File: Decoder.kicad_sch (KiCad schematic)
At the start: 10 parts, among them P1 IO_ADDR, P17 RTC_IO_ADDR, U2 74LS14, U21 74LS682N, U33 74LS10, U39 74LS04, U57 74LS682N, U58 74LS138, U68 74LS138, U7 74LS32

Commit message: rev 1.0
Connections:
- net /CS_FP: now reaches U58.13 (O2)
- net EXTIORQ renamed /INTIORQ
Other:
- note added: "80-83 8242 KBD 84-87 PPI2 88-8B open 8C-8F FDC 90-93 UTIL 94-97 ACRRCS 98-9B VDPCS 9C-9F SNDCS"
- note removed: "80-83 ppi1 84-87 PPI2 88-8B open 8C-8F FDC 90-93 UTIL 94-97 ACRRCS 98-9B VDPCS 9C-9F SNDCS"
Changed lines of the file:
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@@
 	(title_block
 		(title "N8PC")
-		(date "2025-11-02")
-		(rev "000.8")
+		(date "2025-11-26")
+		(rev "000.9")
 		(comment 1 "https://github.com/danwerner21/N8PC")
 		(comment 2 "Based on work by Andrew Lynch and John Coffman")
@@
 		)
 	)
-	(text "80-83 ppi1\n84-87 PPI2\n88-8B open\n8C-8F FDC\n90-93 UTIL\n94-97 ACRRCS\n98-9B VDPCS\n9C-9F SNDCS\n"
+	(text "80-83 8242 KBD\n84-87 PPI2\n88-8B open\n8C-8F FDC\n90-93 UTIL\n94-97 ACRRCS\n98-9B VDPCS\n9C-9F SNDCS\n"
 		(exclude_from_sim no)
 		(at 201.676 70.358 0)
@@
 	)
 	(no_connect
-		(at 166.37 50.8)
+		(at 240.03 184.15)
 	)
 	(no_connect
@@
 		(pts
 			(xy 270.51 104.14) (xy 259.08 104.14)
+		)
+		(stroke
+			(width 0)
+			(type default)
+		)
+	)
+	(wire
+		(pts
+			(xy 166.37 50.8) (xy 180.34 50.8)
 		)
 		(stroke
@@
 		)
 	)
+	(global_label "{slash}CS_FP"
+		(shape output)
+		(at 180.34 50.8 0)
+		(fields_autoplaced yes)
+		(effects
+			(font
+				(size 1.27 1.27)
+			)
+			(justify left)
+		)
+		(property "Intersheetrefs" "${INTERSHEET_REFS}"
+			(at 189.8072 50.8 0)
+			(effects
+				(font
+					(size 1.27 1.27)
+				)
+				(justify left)
+				(hide yes)
+			)
+		)
+	)
 	(global_label "{slash}M1"
 		(shape input)
@@
 		)
 	)
-	(global_label "EXTIORQ"
+	(global_label "{slash}INTIORQ"
 		(shape output)
 		(at 134.62 67.31 0)
@@
 		)
 		(property "Intersheetrefs" "${INTERSHEET_REFS}"
-			(at 144.8129 67.31 0)
+			(at 145.7202 67.31 0)
 			(effects
 				(font

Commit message: V1
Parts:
- removed P17: RTC_IO_ADDR, Custom:STD_DDW_PINHEAD_V_2x04, symbol Connector_Generic:Conn_02x04_Odd_Even
- added P16: IO_ADDR2, Custom:STD_DDW_PinHeader_2x03, symbol Connector_Generic:Conn_02x03_Odd_Even
- added unit 5 of U39
- added U5: 74LS02, Custom:STD_DDW_DIP14, symbol 74xx:74LS02
- added U9: 74LS138, Custom:STD_DDW_DIP16, symbol 74xx:74LS138
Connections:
- net A4: now also U9.3 (A2); no longer U21.8 (P3)
- net GND: now also U21.12 (Q4), U21.13 (P5), P16.1 (Pin_1), P16.3 (Pin_3), P16.5 (Pin_5), U9.1 (A0), U9.2 (A1), U9.5 (E2), U9.8 (GND)
- net VCC: now also U21.9 (Q3), U9.16 (VCC), U9.6 (E3); no longer U21.12 (Q4)
- net /CS_RTC: now also U9.11 (O4); no longer U21.19 (~{P=Q})
- net /INTIORQ: now also U39.10; no longer U57.19 (~{P=Q}), U58.4 (E1)
- net /IORQ: now also U21.11 (P4); no longer U21.13 (P5)
- net /M1: now also U21.8 (P3); no longer U21.11 (P4)
- net /SNDCS: now also U9.15 (O0); no longer U58.7 (O7)
- net at U21.3 (Q0): now also P16.2 (Pin_2)
- net at U21.5 (Q1): now also P16.4 (Pin_4)
- net at U21.7 (Q2): now also P16.6 (Pin_6)
- new net: U39.11, U5.4
- new net /INTIORQ1: U5.5, U57.19 (~{P=Q}), U58.4 (E1)
- new net /INTIORQ2: U21.19 (~{P=Q}), U5.6, U9.4 (E1)
- no-connect marks 10 -> 17
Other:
- note added: "*"
- note added: "* *"
- note added: "80-83 8242 KBD 84-87 PPI2 88-8B FRONT PANEL SWITCHES 8C-8F FDC 90-93 UTIL 94-97 ACRRCS 98-9B VDPCS 9C-9F SPARE A0-A3(AF) SNDCS B0-BF RTC"
- note added: "IO BLOCK IS 64 ADDRESSES LONG EACH OF EIGHT CHIP SELECTS YIELDS FOUR IO ADDRESS RANGE"
- note removed: "80-83 8242 KBD 84-87 PPI2 88-8B open 8C-8F FDC 90-93 UTIL 94-97 ACRRCS 98-9B VDPCS 9C-9F SNDCS"
- note removed: "IO BLOCK IS 32 ADDRESSES LONG EACH OF EIGHT CHIP SELECTS YIELDS FOUR IO ADDRESS RANGE"
- moved on the sheet: U21

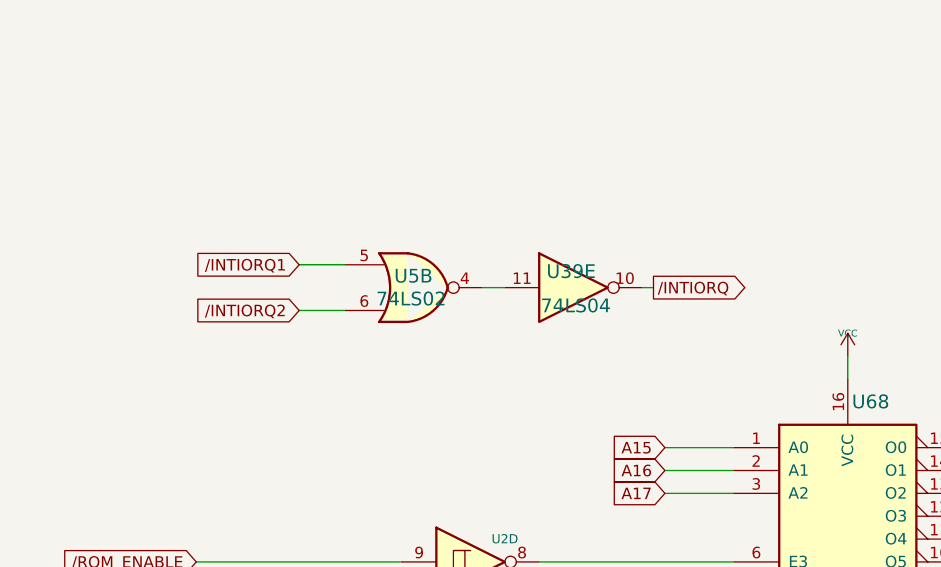
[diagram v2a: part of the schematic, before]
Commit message: V1.1 PCB and schematic fix issue with data direction for bus
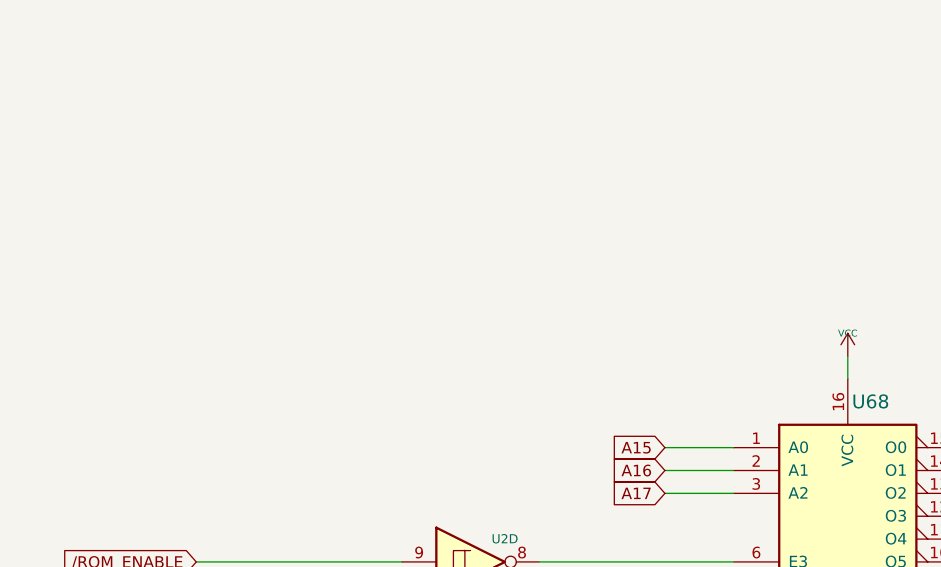
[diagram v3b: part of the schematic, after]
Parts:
- removed unit 5 of U39
- removed U5: 74LS02, Custom:STD_DDW_DIP14, symbol 74xx:74LS02
